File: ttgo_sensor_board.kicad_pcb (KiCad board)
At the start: 2 copper layers, 40 x 38.5 mm, 56 parts, among them J1 Conn_01x13_Female, J2 Conn_01x13_Female, J3 Conn_01x03_Female, J4 Conn_01x03_Female, J5 Conn_01x04_Female, J6 Conn_01x04_Female, J7 Conn_01x04_Female, Q1 Q_NMOS_GSD, Q2 Q_NMOS_GSD, U1 BME680, U2 TCA9800, U3 TLV70218_SOT23-5, U4 LSM6DS3, U5 VEML7700

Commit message: backup current state
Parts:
- added TP12: TestPoint, TestPoint:TestPoint_Pad_D1.0mm, F.Cu at (85.5, 65.8)
- added TP13: TestPoint, TestPoint:TestPoint_Pad_D1.0mm, F.Cu at (93.2, 66.0)
- D3: value USER0 -> U0
- D4: value USER1 -> U1
- R2: value 290 -> 294
- TP1, TP2, TP3, TP4, TP5, TP6, TP7: footprint TestPoint:TestPoint_Pad_D1.5mm -> TestPoint:TestPoint_Pad_D1.0mm
- moved TP6 42.5 mm to (89.8, 87.5), turned to 180 degrees
- moved TP7 42.1 mm to (90.5, 85.2), turned to -90 degrees
- moved TP2 39.3 mm to (89.0, 75.5)
- moved TP3 38.4 mm to (93.8, 76.3)
- moved R8 17.4 mm to (91.3, 76.3), turned to 180 degrees
- moved R7 17.2 mm to (87.0, 76.3), turned to 180 degrees
- moved D4 16.4 mm to (82.0, 74.8), turned to 180 degrees
- moved C11 15.7 mm to (83.0, 64.2)
- moved U5 15.7 mm to (82.7, 61.1)
- moved D3 13.4 mm to (82.0, 73.0), turned to 180 degrees
- moved C10 11.6 mm to (89.0, 66.2)
- moved U4 11.6 mm to (88.8, 63.0)
- moved C9 11.6 mm to (92.2, 62.9)
- moved Q2 11.5 mm to (91.5, 73.8), turned to 0 degrees
- moved Q1 11.2 mm to (87.2, 73.8), turned to 0 degrees
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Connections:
- J2 pad 11: GND -> /GPIO00
- J2 pad 12: /VCC5 -> /GPIO04
- TP2 pad 1: /GPIO36 -> Net-(Q1-Pad3)
- TP3 pad 1: /GPIO39 -> Net-(Q2-Pad3)
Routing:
- net /EN1V8: track 0.00 -> 49.2 mm, vias 0 -> 1
- net /VCC5: track 12.4 -> 55.8 mm, vias 0 -> 1
- net /GPIO22: track 18.0 -> 54.5 mm, vias 0 -> 2
- net /VCC18: track 58.7 -> 93.1 mm, vias 4 -> 8
- net /GPIO21: track 24.0 -> 52.8 mm
- net /GPIO03: track 0.00 -> 26.6 mm
- net /GPIO01: track 0.00 -> 19.1 mm
- net /VCC33: track 41.3 -> 57.2 mm, vias 0 -> 2
- net /GPIO34: track 0.00 -> 14.2 mm
- net /GPIO35: track 0.00 -> 11.3 mm
- net GND: track 49.4 -> 59.9 mm, vias 32 -> 41
- net Net-(D4-Pad1): track 0.00 -> 9.61 mm
- net /SDA1V8: track 40.6 -> 48.6 mm, vias 1 -> 2
- net /SCL1V8: track 37.5 -> 43.8 mm, vias 3 -> 4
- net Net-(D3-Pad1): track 0.00 -> 5.55 mm
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- added copper zone on F.Cu, net GND
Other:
- board text added: "Maurice 03/2023"
- board text added: "Sensorboard v1.0"

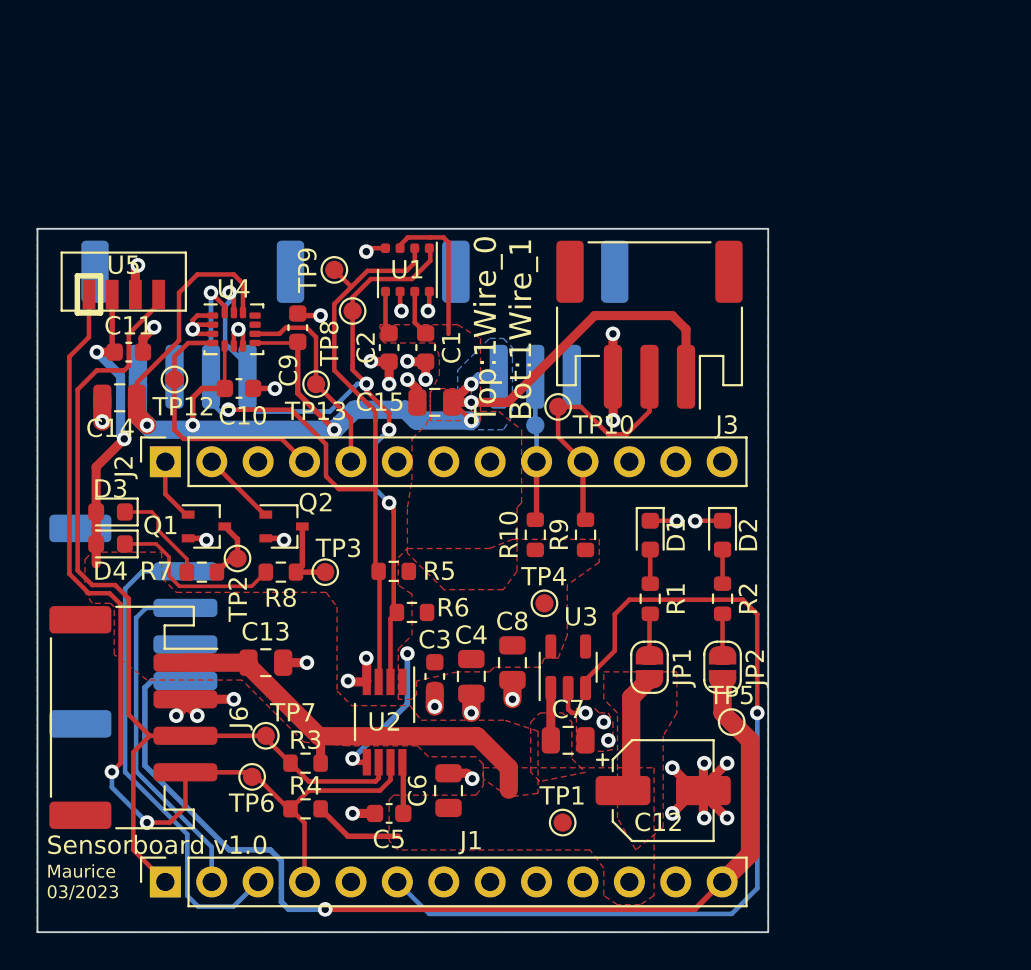
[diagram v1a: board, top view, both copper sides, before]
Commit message: moved leds and change silkscreen
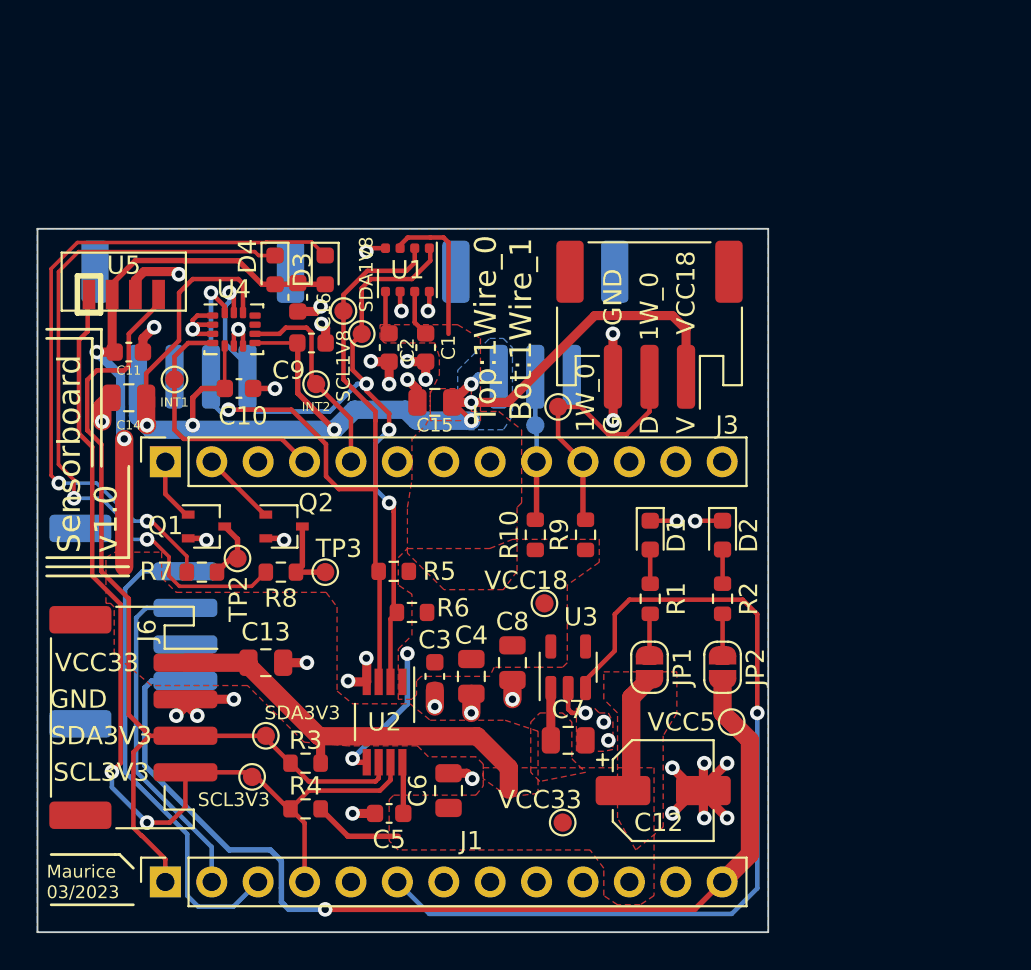
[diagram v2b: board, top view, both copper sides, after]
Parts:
- added C16: 100nF, Capacitor_SMD:C_0603_1608Metric, F.Cu at (92.2, 61.2)
- TP1: value TestPoint -> VCC33
- TP10: value TestPoint -> 1W_0
- TP11: value TestPoint -> 1W_1
- TP12: value TestPoint -> INT1
- TP13: value TestPoint -> INT2
- TP4: value TestPoint -> VCC18
- TP5: value TestPoint -> VCC5
- TP6: value TestPoint -> SCL3V3
- TP7: value TestPoint -> SDA3V3
- TP8: value TestPoint -> SCL1V8
- TP9: value TestPoint -> SDA1V8
- moved D3 17.7 mm to (93.8, 59.8), turned to -90 degrees
- moved D4 17.5 mm to (91.0, 59.8), turned to -90 degrees
- moved TP9 2.30 mm to (94.8, 62.0)
- moved TP8 1.35 mm to (95.8, 63.2)
- moved C9 1.12 mm to (93.0, 63.8), turned to 0 degrees
- moved C14 0.50 mm to (83.0, 66.8)
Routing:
- net Net-(D3-Pad1): track 5.55 -> 37.4 mm, vias 0 -> 2
- net Net-(D4-Pad1): track 9.61 -> 39.0 mm, vias 0 -> 2
- net /VCC33: track 57.2 -> 70.0 mm
- net GND: track 59.9 -> 63.1 mm, vias 41 -> 42
- net /SDA1V8: track 48.6 -> 46.9 mm
- net /GPIO21: track 52.8 -> 51.7 mm
- net /GPIO22: track 54.5 -> 53.4 mm
- net /VCC18: track 93.1 -> 92.5 mm
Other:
- board text added: "1W_0"
- board text added: "D"
- board text added: "G"
- board text added: "GND"
- board text added: "SCL3V3"
- board text added: "SDA3V3"
- board text added: "V"
- board text added: "VCC18"
- board text added: "VCC33"

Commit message: production state
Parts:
- R2: value 294 -> 300
- R7, R8: value 120 -> 82
- TP2: value TestPoint -> USER0
- TP3: value TestPoint -> USER1
- moved TP10 5.10 mm to (111.5, 68.2)
- moved C13 1.41 mm to (89.5, 82.2), turned to -90 degrees
- moved TP7 1.25 mm to (89.2, 85.2)
- moved TP6 0.56 mm to (89.2, 87.2)
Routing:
- net /VCC33: track 70.0 -> 52.1 mm
- net /1WIRE_DATA0: track 14.8 -> 10.4 mm
- net GND: track 63.1 -> 60.6 mm, vias 42 -> 41
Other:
- board text added: "1wire_1"
- board text added: "Bot"
- board text added: "G D V"
- board text added: "I2C 1V8"
- board text added: "RXD TXD G V"
- board text added: "SCL SDA G V"
- board text added: "Top"
- board text added: "UART"
- board text added: "VCC"
- board text removed: "D"
- board text removed: "G"
- board text removed: "V"
